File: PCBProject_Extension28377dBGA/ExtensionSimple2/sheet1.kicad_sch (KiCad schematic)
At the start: 88 parts, among them J1 Conn_02x05_Odd_Even, J1 Conn_02x08_Top_Bottom, J2 Conn_01x02_Pin, Q1 FMMT618TA, U1 SN74ABT541, U2 SN74ABT541

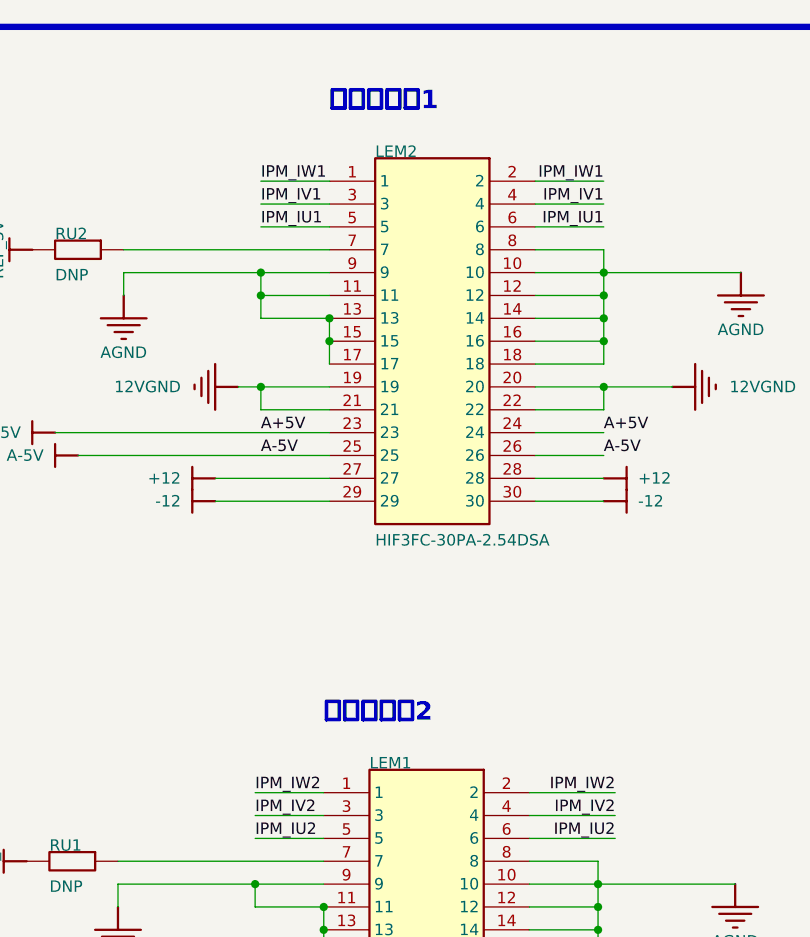
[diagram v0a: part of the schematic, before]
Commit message: add some text items
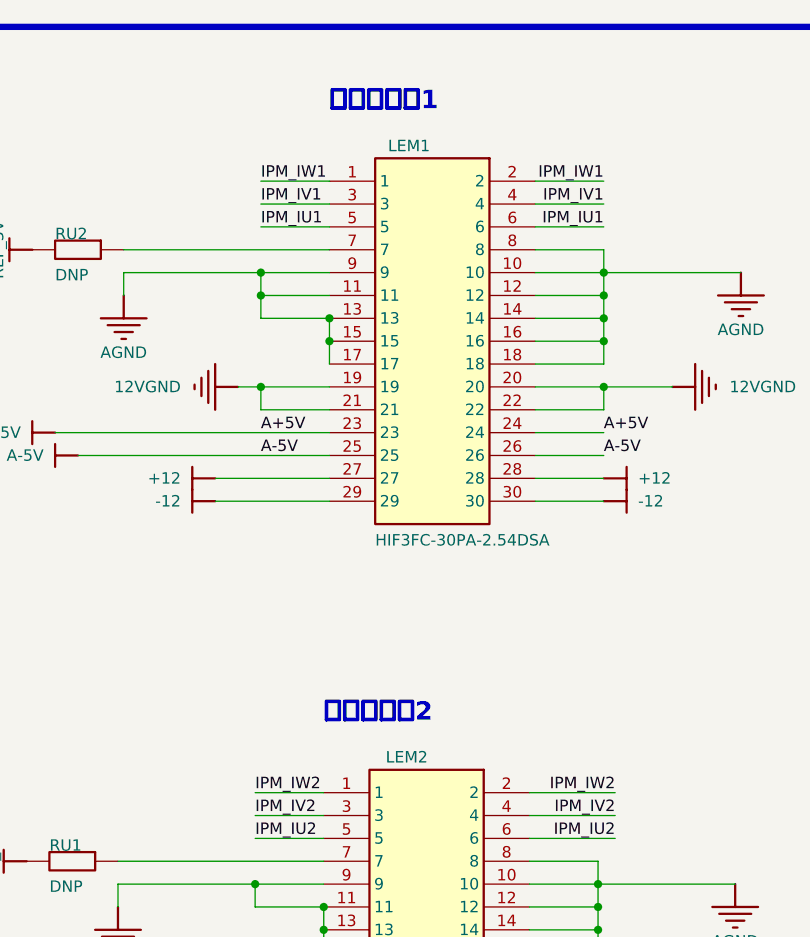
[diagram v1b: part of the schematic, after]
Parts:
- renumbered LEM2 to LEM1, LEM1 to LEM2
